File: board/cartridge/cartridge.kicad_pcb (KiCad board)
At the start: 4 copper layers, 58.4 x 56 mm, 42 parts, among them J1 TF-115-BCP9, J2 HC-TYPE-C-16P-01B, P1 Card Edge, SW1 K3-1410S, SW2 K3-1410S, U1 AMS1117-3.3, U2 ESP32-S3-WROOM-1U, U3 TUSB320, U4 TXS0108E, U5 74LVC245, U6 74LVT14, U7 74LVC541, U8 74LVC541, U9 PCM5100

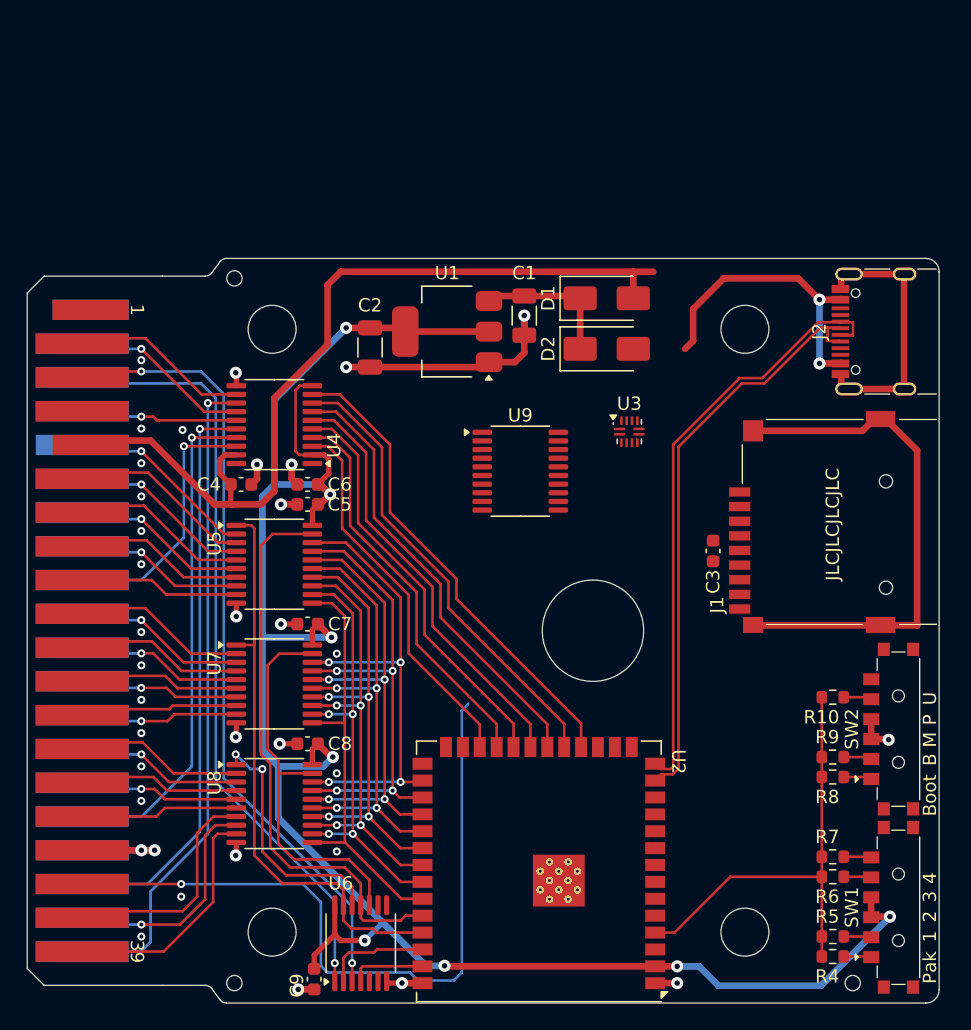
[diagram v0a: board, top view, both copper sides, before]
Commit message: Re-route CoCo bus with all 74-245s.
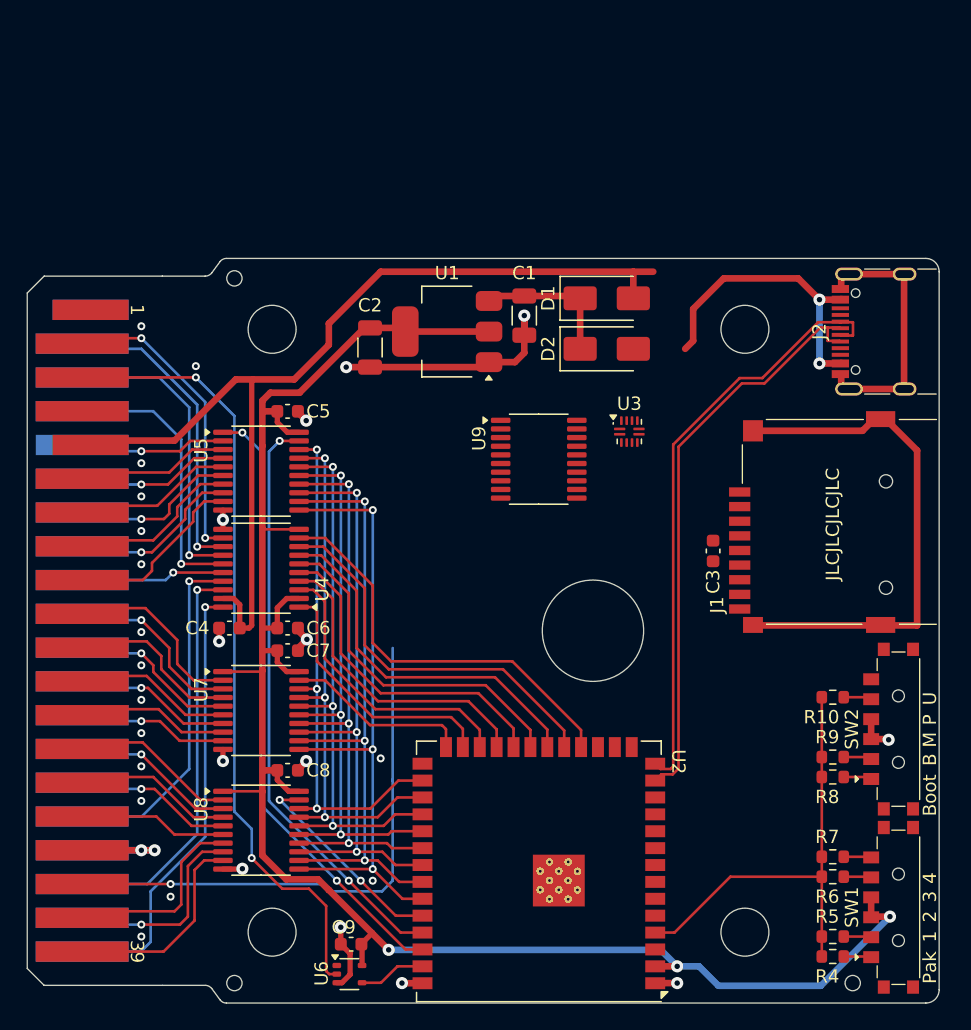
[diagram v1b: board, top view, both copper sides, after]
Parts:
- U6: value 74LVT14 -> 74LVC1G17; footprint Package_SO:TSSOP-14_4.4x5mm_P0.65mm -> Package_TO_SOT_SMD:SOT-353_SC-70-5
- U7, U8: value 74LVC541 -> 74LVC245
- moved C6 10.9 mm to (131.0, 99.8), turned to 0 degrees
- moved U4 10.8 mm to (129.0, 95.3)
- moved C4 10.8 mm to (126.6, 99.8), turned to 180 degrees
- moved C5 7.16 mm to (131.0, 83.5), turned to 0 degrees
- moved U5 7.07 mm to (129.0, 88.0)
- moved C9 3.82 mm to (135.8, 123.6), turned to 180 degrees
- moved C7 2.50 mm to (131.0, 101.5), turned to 0 degrees
- moved C8 2.50 mm to (131.0, 110.5), turned to 0 degrees
- moved U6 2.48 mm to (135.7, 125.8), turned to 0 degrees
- moved U7 2.24 mm to (129.0, 106.0)
- moved U8 2.24 mm to (129.0, 115.0)
- moved U9 1.65 mm to (149.9, 87.1)
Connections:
- net /RESET renamed /~{RESET}
- P1 pad 5: /Host/~{RESET} -> /Host/~{RESET}_5
- P1 pad 6: /Host/E -> /Host/E_5
- U2 pad 19: /~{SLENB} -> /~{NMI}
- U2 pad 20: /~{NMI} -> /E
- U2 pad 22: /~{SCS} -> /R/~{W}
- U2 pad 24: /R/~{W} -> /~{SCS}
- U2 pad 25: unconnected-(U2-GPIO48-Pad25) -> /~{SLENB}
- U2 pad 26: unconnected-(U2-GPIO45-Pad26) -> /ADDR_HI_~{EN}
- U2 pad 36: /A/~{D} -> /ADDR_LO_~{EN}
- U2 pad 37: /DI_AH/~{DO_AL} -> /DATA_~{EN}
- U2 pad 38: /~{CLK} -> /DATA_I/~{O}
- U4 pad 1: unconnected-(U4-A1-Pad1) -> /~{SLENB}
- U4 pad 13: /Host/~{SLENB}_5 -> /Host/~{NMI}_5
- U4 pad 14: /Host/~{NMI}_5 -> /Host/E_5
- U4 pad 16: /Host/~{SCS}_5 -> /Host/R/~{W}_5
- U4 pad 18: /Host/R/~{W}_5 -> /Host/~{SCS}_5
- U4 pad 20: unconnected-(U4-B1-Pad20) -> /Host/~{SLENB}_5
- U4 pad 3: /R/~{W} -> /~{SCS}
- U4 pad 5: /~{SCS} -> /R/~{W}
- U4 pad 7: /~{NMI} -> /E
- U4 pad 8: /~{SLENB} -> /~{NMI}
- U5 pad 1: /DI_AH/~{DO_AL} -> /DATA_I/~{O}
- U5 pad 19: /A/~{D} -> /DATA_~{EN}
- U6 pad 1: /Host/E -> unconnected-(U6-NC-Pad1)
- U6 pad 2: /~{CLK} -> /Host/~{RESET}_5
- U6 pad 3: /Host/~{RESET} -> GND
- U6 pad 5: unconnected-(U6-Pad5) -> +3V3
- U7 pad 1: /DI_AH/~{DO_AL} -> +3V3
- U7 pad 19: /Host/D/~{A} -> /ADDR_HI_~{EN}
- U8 pad 1: /Host/DO_AL/~{DI_AH} -> +3V3
- U8 pad 19: /Host/D/~{A} -> /ADDR_LO_~{EN}
- U9 pad 13: unconnected-(U9-BCK-Pad13) -> /Host/I2S_BCK
- U9 pad 14: unconnected-(U9-DIN-Pad14) -> /Host/I2S_DIN
- U9 pad 15: unconnected-(U9-LRCK-Pad15) -> /Host/I2S_LRCK
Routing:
- net /Host/~{RESET}: track 59.7 -> 0.00 mm, vias 2 -> 0
- net /Host/~{RESET}_5: track 0.00 -> 59.3 mm, vias 0 -> 2
- net /Host/E: track 58.3 -> 0.00 mm, vias 1 -> 0
- net /DATA_I/~{O}: track 0.00 -> 46.7 mm, vias 0 -> 2
- net /DATA_~{EN}: track 0.00 -> 44.5 mm, vias 0 -> 2
- net /DI_AH/~{DO_AL}: track 44.1 -> 0.00 mm
- net /A/~{D}: track 42.6 -> 0.00 mm
- net /Host/D/~{A}: track 29.9 -> 0.00 mm
- net /E: track 0.00 -> 27.9 mm
- net /Host/E_5: track 0.00 -> 22.6 mm, vias 0 -> 1
- net /Host/DO_AL/~{DI_AH}: track 18.7 -> 0.00 mm, vias 2 -> 0
- net /Host/~{SLENB}_5: track 49.9 -> 33.7 mm
- net /ADDR_LO_~{EN}: track 0.00 -> 15.8 mm, vias 0 -> 2
- net /H7: track 32.7 -> 48.3 mm, vias 0 -> 3
- net /~{SLENB}: track 34.8 -> 19.7 mm
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
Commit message: Route more peripherals.
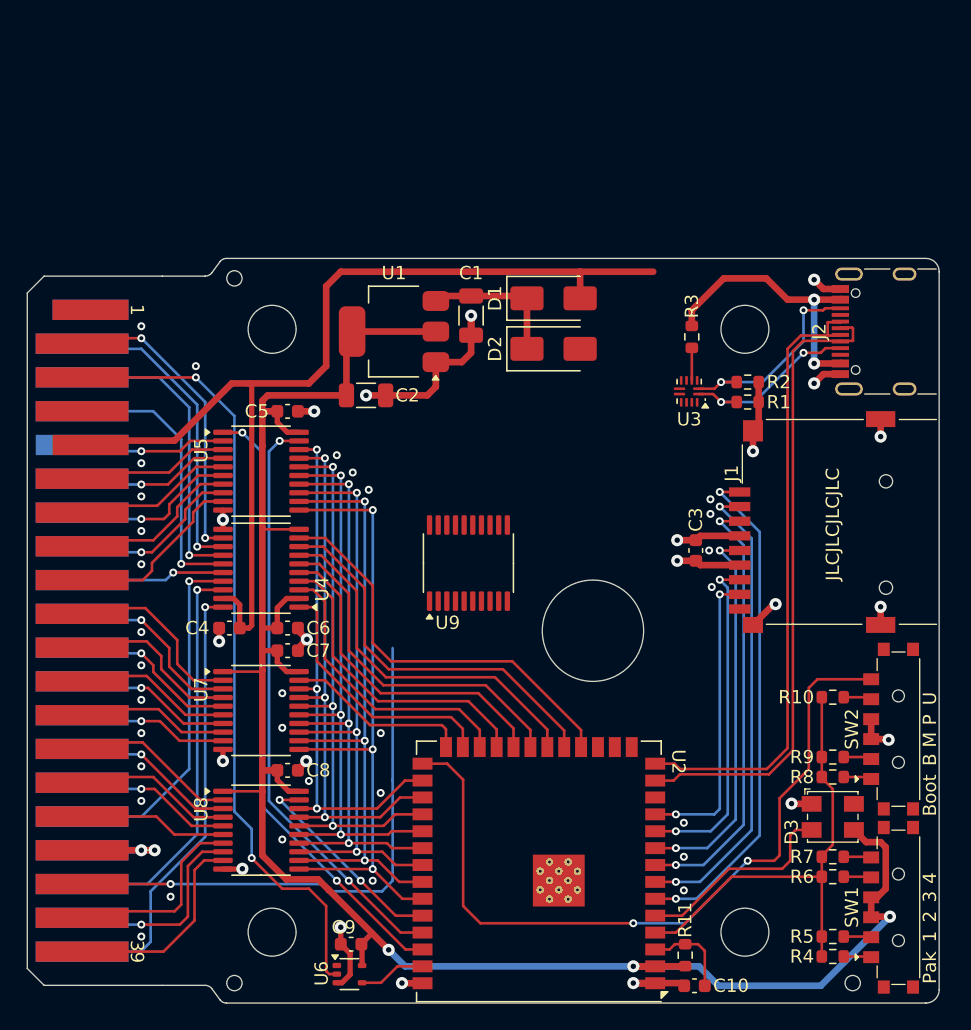
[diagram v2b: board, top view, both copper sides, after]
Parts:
- added C10: 1u, Capacitor_SMD:C_0603_1608Metric, F.Cu at (161.6, 126.7)
- added D3: IN-PI33TBTPRPGP, 0Project:LED_1414_3535Metric, F.Cu at (172.0, 114.0)
- added R1: 5k1, Resistor_SMD:R_0603_1608Metric, F.Cu at (165.6, 82.8)
- added R11: 10k, Resistor_SMD:R_0603_1608Metric, F.Cu at (160.9, 124.4)
- added R2: 5k1, Resistor_SMD:R_0603_1608Metric, F.Cu at (165.6, 81.3)
- added R3: 900k, Resistor_SMD:R_0603_1608Metric, F.Cu at (161.4, 77.9)
- moved U9 9.43 mm to (144.6, 94.9), turned to 90 degrees
- moved U3 5.42 mm to (161.2, 82.0), turned to 180 degrees
- moved C1 4.00 mm to (144.8, 76.3)
- moved D1 4.00 mm to (151.0, 75.0)
- moved D2 4.00 mm to (151.0, 78.8)
- moved U1 4.00 mm to (139.0, 77.5)
- moved C2 3.61 mm to (136.9, 82.3), turned to 0 degrees
- moved C3 1.30 mm to (161.7, 94.0)
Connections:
- SW2 pad 6: /A/~{D}/~{DFU} -> /~{BOOT_USB}
- U2 pad 10: unconnected-(U2-GPIO17-Pad10) -> /SD_DAT0
- U2 pad 11: unconnected-(U2-GPIO18-Pad11) -> /SD_DAT1
- U2 pad 27: unconnected-(U2-GPIO0-Pad27) -> /~{BOOT_USB}
- U2 pad 3: unconnected-(U2-EN-Pad3) -> /ESP_RESET
- U2 pad 5: unconnected-(U2-GPIO5-Pad5) -> /LED
- U2 pad 6: unconnected-(U2-GPIO6-Pad6) -> /SD_DAT2
- U2 pad 7: unconnected-(U2-GPIO7-Pad7) -> /SD_DAT3
- U2 pad 8: unconnected-(U2-GPIO15-Pad8) -> /SD_CMD
- U2 pad 9: unconnected-(U2-GPIO16-Pad9) -> /SD_CLK
- U3 pad 10: unconnected-(U3-GND-Pad10) -> GND
- U3 pad 12: unconnected-(U3-VDD-Pad12) -> +3V3
- U3 pad 4: unconnected-(U3-VBUS_DET-Pad4) -> /VBUS_DET
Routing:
- net /~{BOOT_USB}: track 0.00 -> 58.2 mm, vias 0 -> 2
- net /SD_DAT2: track 0.00 -> 38.4 mm, vias 0 -> 2
- net GND: track 109.3 -> 73.0 mm, vias 31 -> 54
- net /SD_DAT3: track 0.00 -> 35.7 mm, vias 0 -> 2
- net /SD_CMD: track 0.00 -> 33.0 mm, vias 0 -> 2
- net /SD_CLK: track 0.00 -> 29.2 mm, vias 0 -> 2
- net /SD_DAT0: track 0.00 -> 25.4 mm, vias 0 -> 2
- net /SD_DAT1: track 0.00 -> 22.7 mm, vias 0 -> 2
- net /USB_CC2: track 0.00 -> 15.7 mm, vias 0 -> 2
- net /LED: track 0.00 -> 15.5 mm
- net +3V3: track 139.4 -> 153.9 mm, vias 3 -> 4
- net /USB_CC1: track 0.00 -> 13.7 mm, vias 0 -> 2
- net /ESP_RESET: track 0.00 -> 6.73 mm
- net /USB_DM: track 44.2 -> 48.1 mm
- net /VBUS_DET: track 0.00 -> 2.45 mm
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
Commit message: Add a bunch of USB stuff.
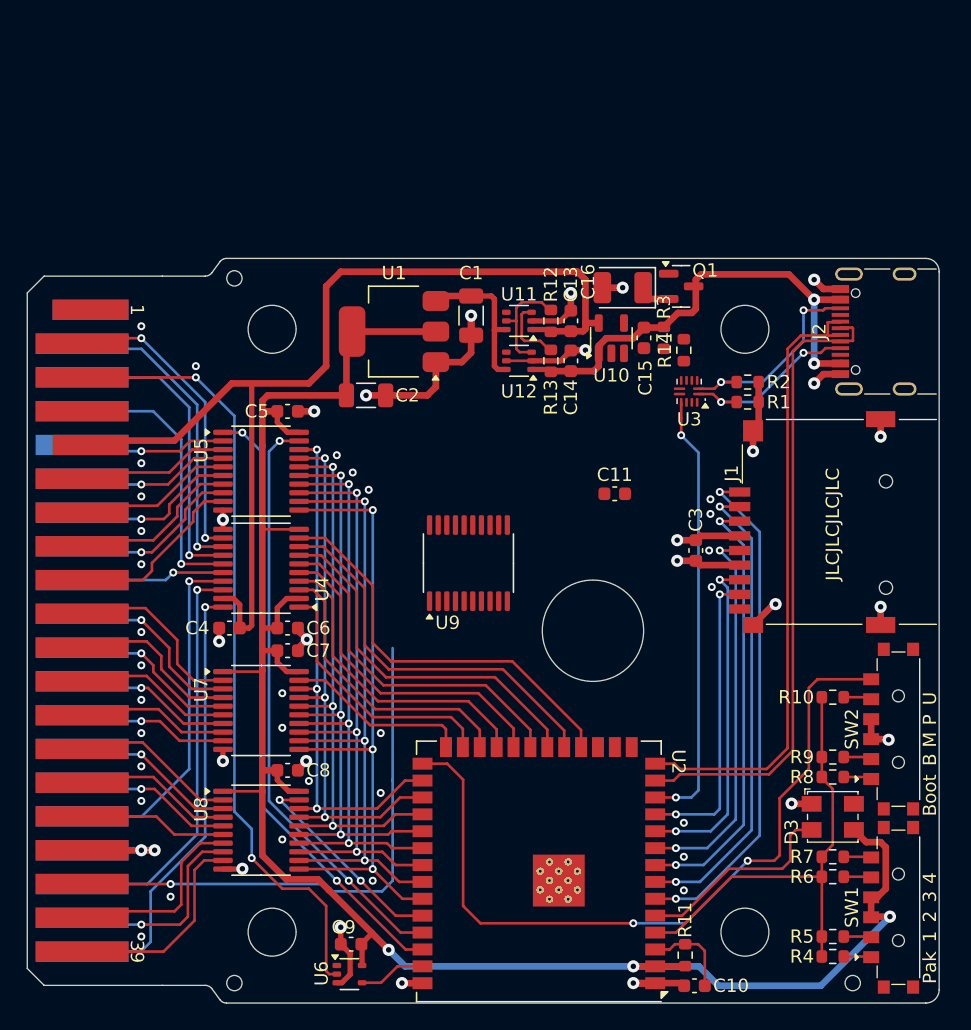
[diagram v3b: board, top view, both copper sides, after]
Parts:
- removed D1, D2: SS14, Diode_SMD:D_SMA
- added C11: 100n, Capacitor_SMD:C_0603_1608Metric, F.Cu at (155.6, 89.7)
- added C13: 1u, Capacitor_SMD:C_0603_1608Metric, F.Cu at (152.3, 76.7)
- added C14: 1u, Capacitor_SMD:C_0603_1608Metric, F.Cu at (152.3, 79.7)
- added C15: 100n, Capacitor_SMD:C_0603_1608Metric, F.Cu at (157.8, 78.0)
- added C16: 150u, Capacitor_Tantalum_SMD:CP_EIA-3528-21_Kemet-B, F.Cu at (156.2, 74.2)
- added Q1: DMG2301L, Package_TO_SOT_SMD:SOT-23, F.Cu at (160.6, 74.1)
- added R12: 10k, Resistor_SMD:R_0603_1608Metric, F.Cu at (150.8, 76.7)
- added R13: 10k, Resistor_SMD:R_0603_1608Metric, F.Cu at (150.8, 79.7)
- added R14: 10k, Resistor_SMD:R_0603_1608Metric, F.Cu at (160.8, 78.9)
- added U10: TPS2041B, Package_TO_SOT_SMD:SOT-23-5, F.Cu at (155.3, 78.0)
- added U11: LM66100DCK, Package_TO_SOT_SMD:SOT-363_SC-70-6, F.Cu at (148.4, 76.7)
- added U12: LM66100DCK, Package_TO_SOT_SMD:SOT-363_SC-70-6, F.Cu at (148.4, 79.7)
- U3: value TUSB320 -> TUSB321
- moved R3 2.10 mm to (159.3, 78.0)
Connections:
- U2 pad 12: unconnected-(U2-GPIO8-Pad12) -> /USB_ID
- U3 pad 12: +3V3 -> +5V
- U3 pad 4: /VBUS_DET -> unconnected-(U3-PORT-Pad4)
- U3 pad 5: unconnected-(U3-ADDR-Pad5) -> /VBUS_DET
- U3 pad 9: unconnected-(U3-ID-Pad9) -> /USB_ID
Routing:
- net /USB_ID: track 0.00 -> 33.2 mm, vias 0 -> 2
- net VBUS: track 20.9 -> 36.2 mm
- net GND: track 73.0 -> 85.4 mm, vias 54 -> 57
- net Net-(U11-ST): track 0.00 -> 8.11 mm
- net Net-(U11-~{CE}): track 0.00 -> 5.17 mm
- net Net-(Q1-S): track 0.00 -> 2.89 mm
- net /VBUS_DET: track 2.45 -> 0.00 mm
- net +5V: track 75.6 -> 78.0 mm
- net /+5V_IN: track 10.9 -> 11.6 mm

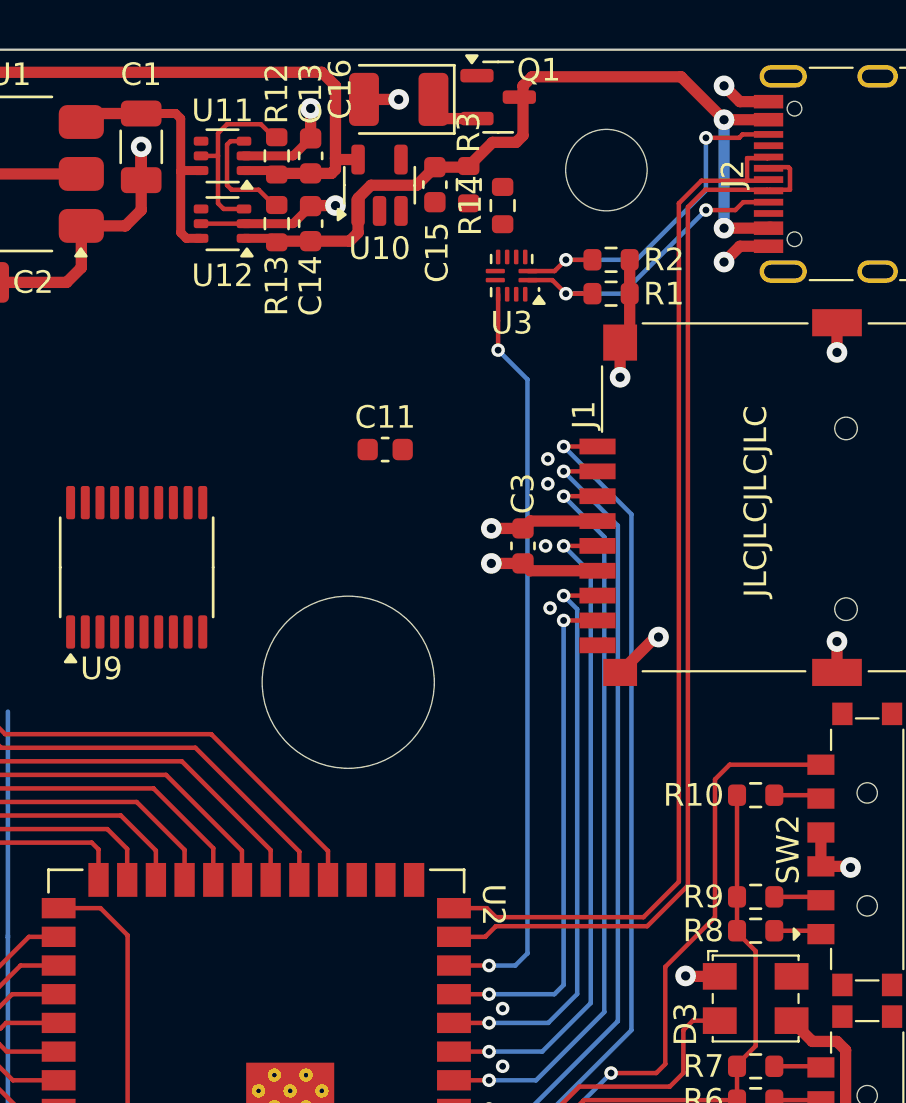
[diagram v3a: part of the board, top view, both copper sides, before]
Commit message: Finish USB power management.
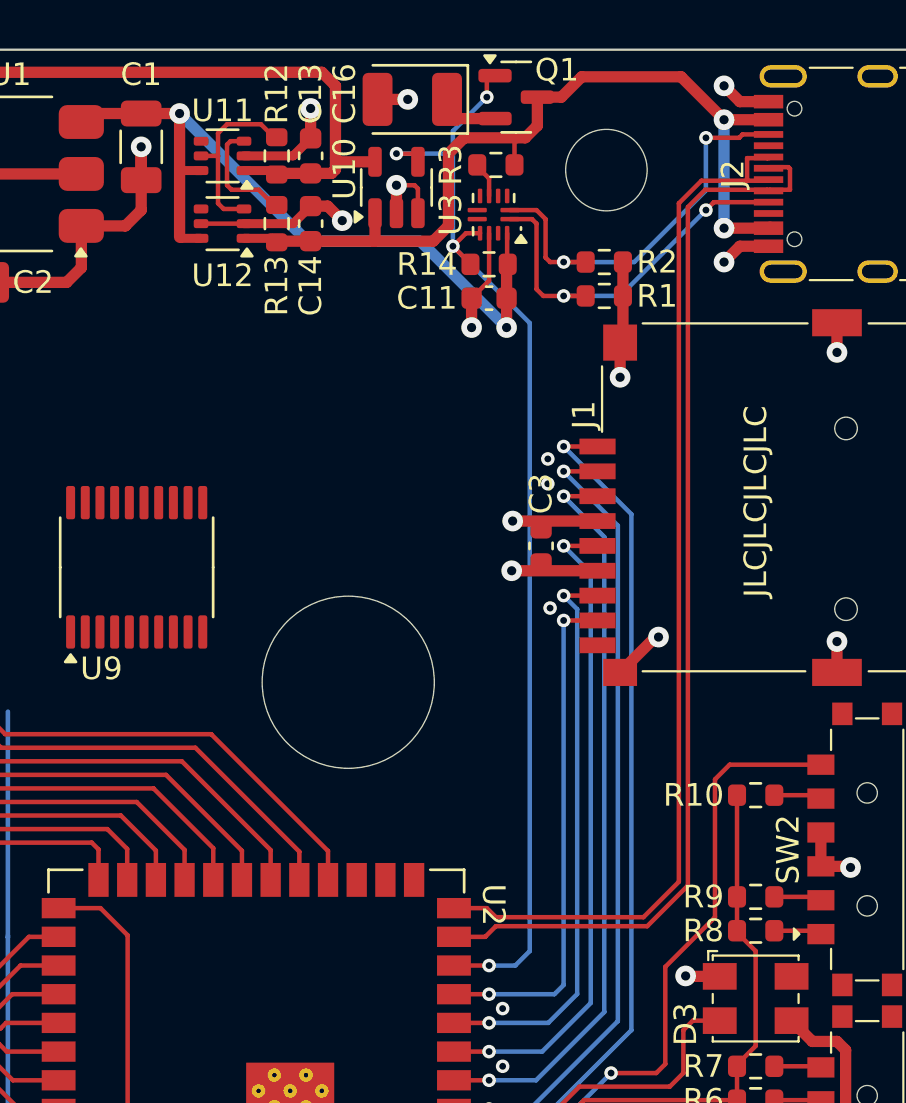
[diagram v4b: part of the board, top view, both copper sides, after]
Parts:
- removed C15: 100n, Capacitor_SMD:C_0603_1608Metric
- Q1: footprint Package_TO_SOT_SMD:SOT-23 -> 0Project:SOT-23
- R14: value 10k -> 100k
- moved C11 8.13 mm to (160.2, 83.0), turned to 180 degrees
- moved U3 2.82 mm to (160.4, 79.3)
- moved R14 2.67 mm to (160.2, 81.5), turned to 0 degrees
- moved R3 1.49 mm to (160.5, 77.1), turned to 0 degrees
- moved C3 0.80 mm to (162.5, 94.0)
- moved Q1 0.80 mm to (161.4, 74.1)
- moved U10 0.76 mm to (156.1, 78.1)
- moved C16 0.60 mm to (156.8, 74.2)
- moved R1 0.32 mm to (165.3, 82.9)
- moved R2 0.32 mm to (165.3, 81.4)
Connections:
- C1 pad 1: /+5V_IN -> +5V
- C13 pad 1: +5V -> +5V_HOST
- C4 pad 1: +5V -> +5V_HOST
- P1 pad 9: +5V -> +5V_HOST
- R12 pad 1: +5V -> +5V_HOST
- U1 pad 3: /+5V_IN -> +5V
- U10 pad 5: +5V -> +5V_HOST
- U11 pad 1: +5V -> +5V_HOST
- U11 pad 6: /+5V_IN -> +5V
- U12 pad 6: /+5V_IN -> +5V
- U4 pad 19: +5V -> +5V_HOST
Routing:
- net +5V_HOST: track 0.00 -> 78.7 mm
- net +5V: track 78.0 -> 34.5 mm, vias 0 -> 2
- net /USB_ID: track 33.2 -> 51.1 mm, vias 2 -> 4
- net /+5V_IN: track 11.6 -> 0.00 mm
- net GND: track 85.4 -> 93.1 mm, vias 57 -> 58
- net /USB_CC1: track 13.7 -> 17.2 mm
- net VBUS: track 36.2 -> 39.2 mm
- net /USB_CC2: track 15.7 -> 18.1 mm
- net /VBUS_DET: track 0.00 -> 1.59 mm
- net +3V3: track 153.9 -> 152.8 mm
